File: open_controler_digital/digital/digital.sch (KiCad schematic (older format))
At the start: 20 parts, among them J1 Conn_02x20_Odd_Even

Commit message: avances en la pcb
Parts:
- removed R? (x2): R, symbol Device:R
- removed U? (x5): PC817, Package_DIP:DIP-4_W7.62mm, symbol Isolator:PC817
- added C?: C, symbol Device:C
- added J?: Conn_01x02, symbol Connector_Generic:Conn_01x02
- added Q?: SSM3J338, symbol mosfet:SSM3J338
- added Q?: BC556, Package_TO_SOT_THT:TO-92_Inline, symbol Transistor_BJT:BC556
- added R? (x3): 2K2, symbol Device:R
- added R?: 7R, symbol Device:R
- added R?: 10K, symbol Device:R
- added U?: PC817, Package_DIP:DIP-4_W7.62mm, symbol Isolator:PC817
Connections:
- net labels added: Vcc_1
- net labels removed: GND_B, OD_00
- wire segments 103 -> 95
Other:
- note removed: "temperature buses"
- moved on the sheet: J?, R?

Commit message: avances en la pcb
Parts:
- added Q?: BC556, Package_TO_SOT_THT:TO-92_Inline, symbol Transistor_BJT:BC556
- added R?: 9R, symbol Device:R
- added R?: xxK, symbol Device:R
- added R?: 120R, symbol Device:R
- R?: value 7R -> 4R
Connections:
- wire segments 95 -> 102
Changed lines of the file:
@@
 P 6700 1050
 F 0 "R?" H 6770 1096 50  0000 L CNN
-F 1 "7R" H 6770 1005 50  0000 L CNN
+F 1 "4R" H 6770 1005 50  0000 L CNN
 F 2 "" V 6630 1050 50  0001 C CNN
 F 3 "~" H 6700 1050 50  0001 C CNN
@@
 	6940 1600 7300 1600
 Connection ~ 6940 1600
+$Comp
+L Transistor_BJT:BC556 Q?
+U 1 1 62AE7003
+P 12590 1090
+F 0 "Q?" H 12500 960 50  0000 L CNN
+F 1 "BC556" H 12700 900 50  0000 L CNN
+F 2 "Package_TO_SOT_THT:TO-92_Inline" H 12790 1015 50  0001 L CIN
+F 3 "http://www.fairchildsemi.com/ds/BC/BC557.pdf" H 12590 1090 50  0001 L CNN
+	1    12590 1090
+	-1   0    0    1
+$EndComp
+$Comp
+L Device:R R?
+U 1 1 62AE7009
+P 12790 940
+F 0 "R?" H 12890 990 50  0000 L CNN
+F 1 "9R" H 12890 890 50  0000 L CNN
+F 2 "" V 12720 940 50  0001 C CNN
+F 3 "~" H 12790 940 50  0001 C CNN
+	1    12790 940
+	1    0    0    -1
+$EndComp
+Wire Wire Line
+	12490 890  12490 790
+Wire Wire Line
+	12490 790  12790 790
+Connection ~ 12490 790
+$Comp
+L Device:R R?
+U 1 1 62AE7021
+P 12790 1240
+F 0 "R?" H 12890 1260 50  0000 L CNN
+F 1 "xxK" H 12900 1170 50  0000 L CNN
+F 2 "" V 12720 1240 50  0001 C CNN
+F 3 "~" H 12790 1240 50  0001 C CNN
+	1    12790 1240
+	1    0    0    -1
+$EndComp
+Text GLabel 12490 1790 0    50   Input ~ 0
+GND_1
+Wire Wire Line
+	12490 790  12490 600
+Text GLabel 12490 600  0    50   Input ~ 0
+Vcc_1
+$Comp
+L Device:R R?
+U 1 1 62AE7034
+P 12490 1440
+F 0 "R?" H 12240 1510 50  0000 L CNN
+F 1 "120R" H 12220 1410 50  0000 L CNN
+F 2 "" V 12420 1440 50  0001 C CNN
+F 3 "~" H 12490 1440 50  0001 C CNN
+	1    12490 1440
+	1    0    0    -1
+$EndComp
+Connection ~ 12790 1090
+Wire Wire Line
+	12490 1590 12490 1640
+Wire Wire Line
+	12790 1390 12790 1640
+Wire Wire Line
+	12490 1640 12790 1640
+Wire Wire Line
+	12490 1640 12490 1790
+Connection ~ 12490 1640
 $EndSCHEMATC

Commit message: desarrollando hw, limitador de intensidad
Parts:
- removed Q?: SSM3J338, symbol mosfet:SSM3J338
- removed Q?: BC556, Package_TO_SOT_THT:TO-92_Inline, symbol Transistor_BJT:BC556
- removed R? (x4): R, symbol Device:R
- removed R? (x2): 2K2, symbol Device:R
- added C? (x7): C, symbol Device:C
- added D? (x9): BZT52Bxx, Diode_SMD:D_SOD-123, symbol Diode:BZT52Bxx
- added Q? (x8): BC856, Package_TO_SOT_SMD:SOT-23, symbol Transistor_BJT:BC856
- added Q? (x8): VP0610T, Package_TO_SOT_SMD:SOT-23, symbol Transistor_FET:VP0610T
- added R? (x17): 2K2, symbol Device:R
- added R? (x7): 4R, symbol Device:R
- added R? (x7): 10K, symbol Device:R
- added U? (x8): PC817, Package_DIP:DIP-4_W7.62mm, symbol Isolator:PC817
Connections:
- wire segments 102 -> 243
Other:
- note added: "La resistencia elevada para que el consumo , en condiciones normales de trabajo, sea bajo\nResistencia baja para asegurar la estabilidad del circuito y eliminar efectos de ruido\nEl Zener puede ir desde 3,5V a 20V que es el maximo de sopore de jmosfet"
- moved on the sheet: C?, J1, J?, R?, U?

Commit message: avanzando con el limitador de intensidad
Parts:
- removed C? (x5): C, symbol Device:C
- removed D? (x9): BZT52Bxx, Diode_SMD:D_SOD-123, symbol Diode:BZT52Bxx
- removed Q?: BC556, Package_TO_SOT_THT:TO-92_Inline, symbol Transistor_BJT:BC556
- removed Q? (x5): BC856, Package_TO_SOT_SMD:SOT-23, symbol Transistor_BJT:BC856
- removed Q? (x5): VP0610T, Package_TO_SOT_SMD:SOT-23, symbol Transistor_FET:VP0610T
- removed R? (x6): R, symbol Device:R
- removed R?: 9R, symbol Device:R
- removed R?: xxK, symbol Device:R
- removed R?: 120R, symbol Device:R
- removed R? (x12): 2K2, symbol Device:R
- removed R? (x5): 4R, symbol Device:R
- removed R? (x5): 10K, symbol Device:R
- removed U? (x6): PC817, Package_DIP:DIP-4_W7.62mm, symbol Isolator:PC817
- added C? (x3): C, symbol Device:C
- added Q? (x3): BC856, Package_TO_SOT_SMD:SOT-23, symbol Transistor_BJT:BC856
- added Q? (x3): VP0610T, Package_TO_SOT_SMD:SOT-23, symbol Transistor_FET:VP0610T
- added R? (x9): 10K, symbol Device:R
- added R? (x16): 4K7, symbol Device:R
- added R? (x6): 2K2, symbol Device:R
- added R? (x3): 7R, symbol Device:R
- added U? (x11): PC817, Package_DIP:DIP-4_W7.62mm, symbol Isolator:PC817
- J?: value Conn_01x10 -> d_o_01x10
- J?: value Conn_01x10 -> d_i_01x10
- R? (x3): value 4R -> 7R
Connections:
- net labels added: GND_xx, GPIO_xx, d_i_0, d_i_1, d_i_2, d_i_3, d_i_4, d_i_5, d_o_0, d_o_1, d_o_2, d_o_3, d_o_4, d_o_5, id_xx
- wire segments 243 -> 168
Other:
- note removed: "La resistencia elevada para que el consumo , en condiciones normales de trabajo, sea bajo\nResistencia baja para asegurar la estabilidad del circuito y eliminar efectos de ruido\nEl Zener puede ir desde 3,5V a 20V que es el maximo de sopore de jmosfet"
- moved on the sheet: C?, J?, Q?, R?, U?

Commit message: avances pcb digital
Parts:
- removed C?: C, symbol Device:C
- removed Q?: BC856, Package_TO_SOT_SMD:SOT-23, symbol Transistor_BJT:BC856
- removed Q?: VP0610T, Package_TO_SOT_SMD:SOT-23, symbol Transistor_FET:VP0610T
- removed R? (x2): 10K, symbol Device:R
- removed R? (x2): 2K2, symbol Device:R
- removed R?: 7R, symbol Device:R
- removed R? (x6): 4K7, symbol Device:R
- removed U? (x4): PC817, Package_DIP:DIP-4_W7.62mm, symbol Isolator:PC817
- added C2, C7: C, Capacitor_SMD:C_1206_3216Metric_Pad1.42x1.75mm_HandSolder, symbol Device:C
- added D1: D_Schottky, Diode_SMD:D_2114_3652Metric, symbol Device:D_Schottky
- added Q2: BC856, Package_TO_SOT_SMD:SOT-23, symbol Transistor_BJT:BC856
- added Q4: VP0610T, Package_TO_SOT_SMD:SOT-23, symbol Transistor_FET:VP0610T
- added R10: 1K5, Resistor_SMD:R_1206_3216Metric_Pad1.42x1.75mm_HandSolder, symbol Device:R
- added R2: 7R, Resistor_SMD:R_1206_3216Metric_Pad1.42x1.75mm_HandSolder, symbol Device:R
- added R36, R42: 4K7, Resistor_SMD:R_1206_3216Metric_Pad1.42x1.75mm_HandSolder, symbol Device:R
- added R4, R8: 10K, Resistor_SMD:R_1206_3216Metric_Pad1.42x1.75mm_HandSolder, symbol Device:R
- added R6: 1K2, Resistor_SMD:R_1206_3216Metric_Pad1.42x1.75mm_HandSolder, symbol Device:R
- added U12, U2: PC817, Package_DIP:DIP-4_W8.89mm_SMDSocket_LongPads, symbol Isolator:PC817
- C1, C3, C4, C5, C6: renamed from C?; footprint (none) -> Capacitor_SMD:C_1206_3216Metric_Pad1.42x1.75mm_HandSolder
- J1, J2: renamed from J?; footprint (none) -> Connector_Phoenix_MC:PhoenixContact_MCV_1,5_10-G-3.5_1x10_P3.50mm_Vertical
- J4: renamed from J?; footprint (none) -> Connector_Phoenix_MC:PhoenixContact_MCV_1,5_2-G-3.5_1x02_P3.50mm_Vertical
- R1, R11, R12, R13, R14, R15, R16, R17, R18, R23, R24, R25, R26, R27, R28, R29, R3, R30, R31, R32, R33, R34, R35, R37, R38, R39, R40, R41, R7: renamed from R?; footprint (none) -> Resistor_SMD:R_1206_3216Metric_Pad1.42x1.75mm_HandSolder
- R19, R20, R21, R22, R5: renamed from R?; value 2K2 -> 1K2; footprint (none) -> Resistor_SMD:R_1206_3216Metric_Pad1.42x1.75mm_HandSolder
- R9: renamed from R?; value 2K2 -> 1K5; footprint (none) -> Resistor_SMD:R_1206_3216Metric_Pad1.42x1.75mm_HandSolder
- U1, U10, U11, U3, U4, U5, U6, U7, U8, U9: renamed from U?; footprint Package_DIP:DIP-4_W7.62mm -> Package_DIP:DIP-4_W8.89mm_SMDSocket_LongPads
- gave numbers to parts that had none: 10
- renumbered J1 to J3
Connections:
- net labels added: di20, di21, di22, di30, di31, di32, do00, do01, do02, do10, do11, do12, gi2, gi3, go0, go1, vo0, vo1
- net labels removed: 3v3_1, 3v3_2, GND_xx, GPIO_0, GPIO_1, GPIO_10, GPIO_11, GPIO_14, GPIO_15, GPIO_17, GPIO_2, GPIO_21, GPIO_3, GPIO_4, GPIO_7, GPIO_8, GPIO_9, GPIO_xx, Vcc_1, d_i_0, d_i_1, d_i_2, d_i_3, d_i_4, d_i_5, d_o_0, d_o_1, d_o_2, d_o_3, d_o_4, d_o_5, id_xx
- wire segments 168 -> 169
- no-connect marks 2 -> 18
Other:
- note added: "3v3"
- note added: "3v3_1"
- note added: "5V"
- note added: "GND"
- note added: "GPIO0"
- note added: "GPIO_1"
- note added: "GPIO_10"
- note added: "GPIO_11"
- note added: "GPIO_12"
- note added: "GPIO_13"
- note added: "GPIO_14"
- note added: "GPIO_15"
- note added: "GPIO_16"
- note added: "GPIO_17"
- note added: "GPIO_18"
- note added: "GPIO_19"
- note added: "GPIO_2"
- note added: "GPIO_20"
- note added: "GPIO_21"
- note added: "GPIO_22"
- note added: "GPIO_23"
- note added: "GPIO_24"
- note added: "GPIO_25"
- note added: "GPIO_3"
- note added: "GPIO_4"
- note added: "GPIO_5"
- note added: "GPIO_6"
- note added: "GPIO_7"
- note added: "GPIO_8"
- note added: "GPIO_9"
- note added: "IOT_0"
- note added: "IOT_1"
- moved on the sheet: C6, J1, J2, J4, Q12, Q8, R14, R18, R22, R26, R30, R35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

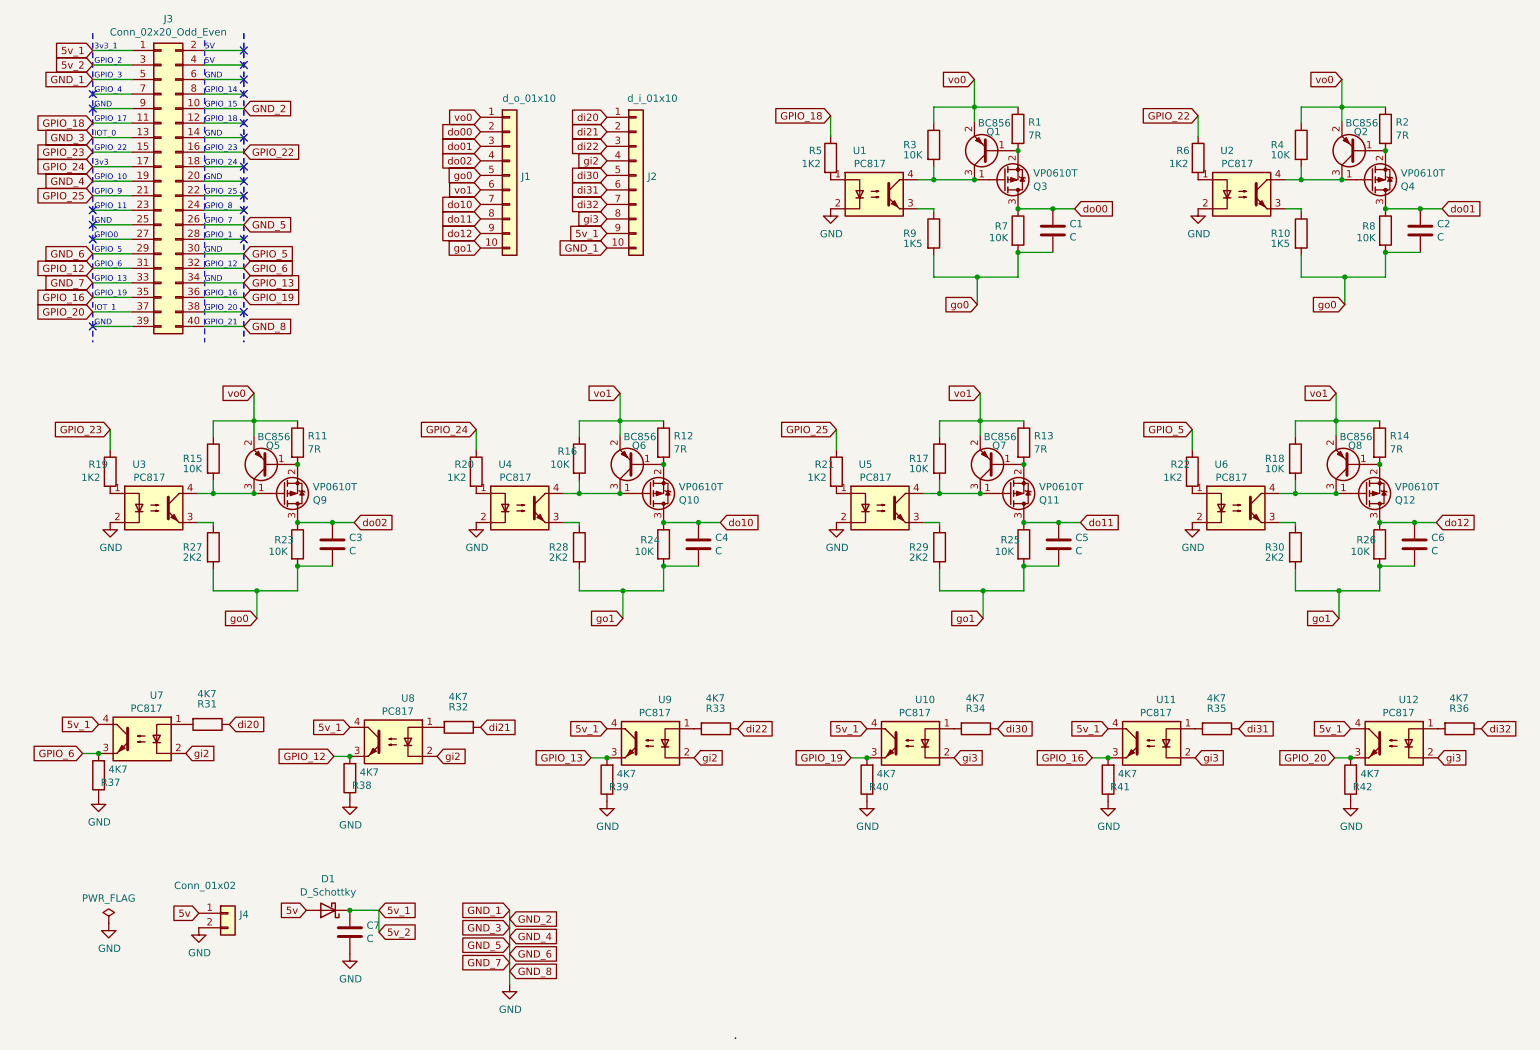
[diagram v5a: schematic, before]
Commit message: desarrollo de la PCB con la huella de la Raspberry
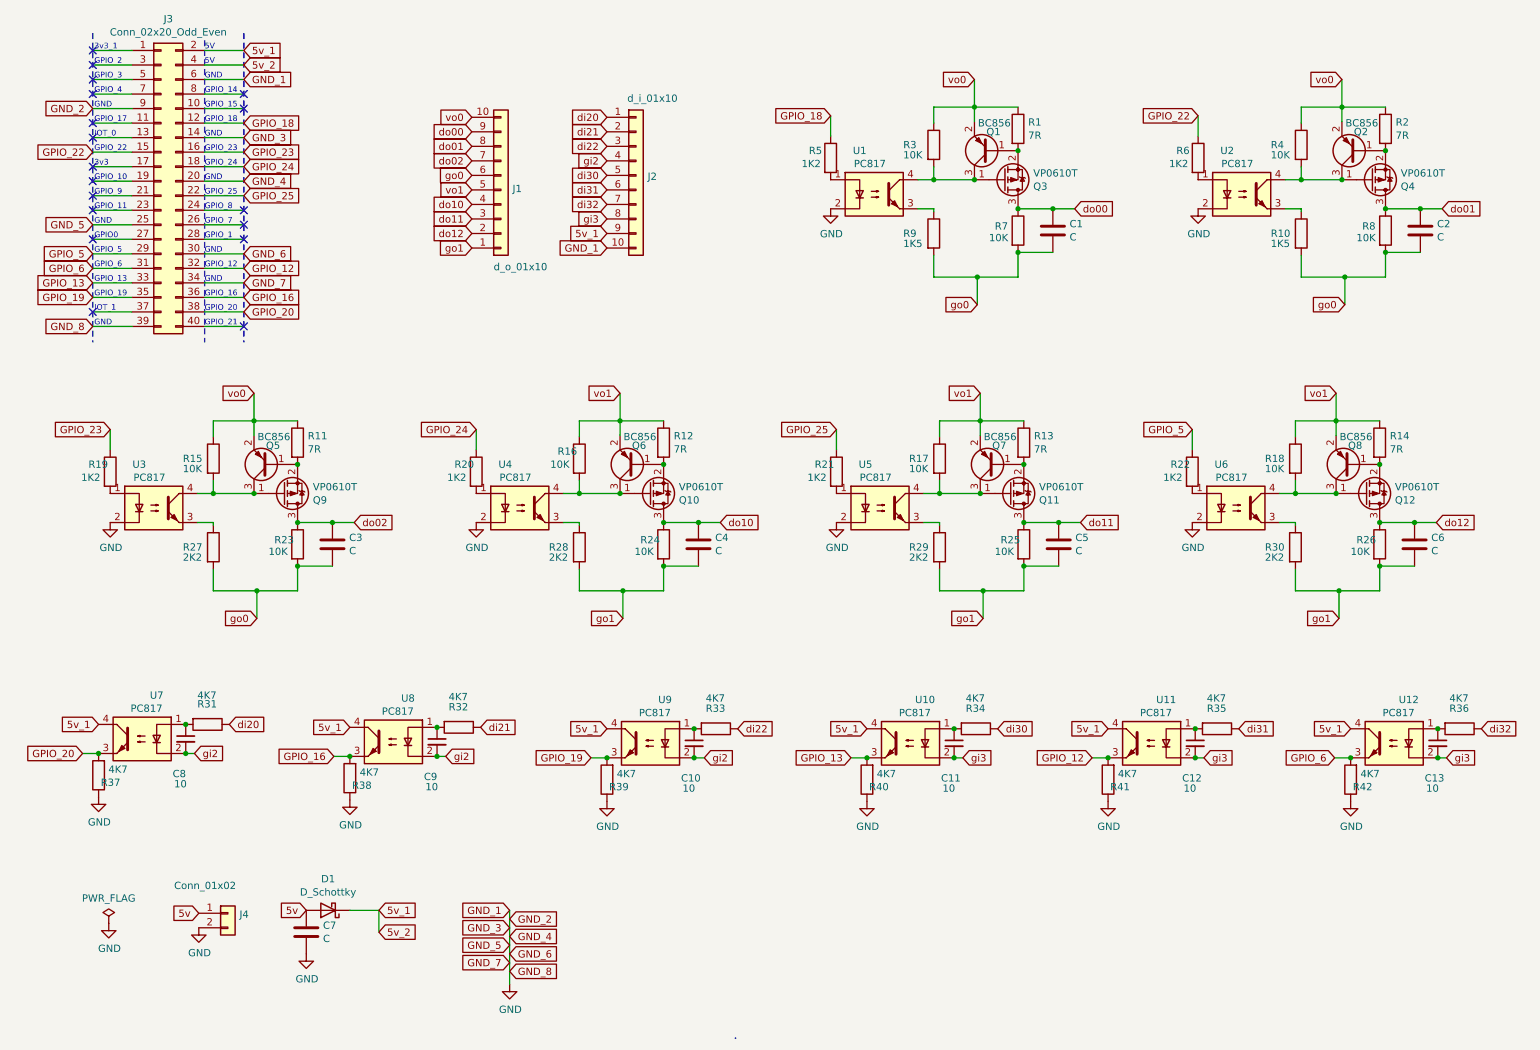
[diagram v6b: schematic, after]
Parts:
- added C10, C11, C12, C13, C8, C9: 10, Capacitor_SMD:C_1206_3216Metric_Pad1.42x1.75mm_HandSolder, symbol Device:C_Small
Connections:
- wire segments 169 -> 175
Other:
- moved on the sheet: C7, J1

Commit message: version para fabricacion
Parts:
- C1, C2, C3, C4, C5, C6, C7: value C -> 10
- Q10, Q11, Q12, Q3, Q4, Q9: value VP0610T -> JM
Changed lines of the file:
@@
 P 7700 2050
 F 0 "C1" H 7815 2096 50  0000 L CNN
-F 1 "C" H 7815 2005 50  0000 L CNN
+F 1 "10" H 7815 2005 50  0000 L CNN
 F 2 "Capacitor_SMD:C_1206_3216Metric_Pad1.42x1.75mm_HandSolder" H 7738 1900 50  0001 C CNN
 F 3 "~" H 7700 2050 50  0001 C CNN
@@
 P 7360 1700
 F 0 "Q3" H 7565 1746 50  0000 L CNN
-F 1 "VP0610T" H 7565 1655 50  0000 L CNN
+F 1 "JM" H 7565 1655 50  0000 L CNN
 F 2 "Package_TO_SOT_SMD:SOT-23" H 7560 1625 50  0001 L CIN
 F 3 "http://www.vishay.com/docs/70209/70209.pdf" H 7360 1700 50  0001 L CNN
@@
 P 2740 4210
 F 0 "C3" H 2855 4256 50  0000 L CNN
-F 1 "C" H 2855 4165 50  0000 L CNN
+F 1 "10" H 2855 4165 50  0000 L CNN
 F 2 "Capacitor_SMD:C_1206_3216Metric_Pad1.42x1.75mm_HandSolder" H 2778 4060 50  0001 C CNN
 F 3 "~" H 2740 4210 50  0001 C CNN
@@
 P 2400 3860
 F 0 "Q9" H 2605 3906 50  0000 L CNN
-F 1 "VP0610T" H 2605 3815 50  0000 L CNN
+F 1 "JM" H 2605 3815 50  0000 L CNN
 F 2 "Package_TO_SOT_SMD:SOT-23" H 2600 3785 50  0001 L CIN
 F 3 "http://www.vishay.com/docs/70209/70209.pdf" H 2400 3860 50  0001 L CNN
@@
 P 4920 3860
 F 0 "Q10" H 5125 3906 50  0000 L CNN
-F 1 "VP0610T" H 5125 3815 50  0000 L CNN
+F 1 "JM" H 5125 3815 50  0000 L CNN
 F 2 "Package_TO_SOT_SMD:SOT-23" H 5120 3785 50  0001 L CIN
 F 3 "http://www.vishay.com/docs/70209/70209.pdf" H 4920 3860 50  0001 L CNN
@@
 P 5260 4210
 F 0 "C4" H 5375 4256 50  0000 L CNN
-F 1 "C" H 5375 4165 50  0000 L CNN
+F 1 "10" H 5375 4165 50  0000 L CNN
 F 2 "Capacitor_SMD:C_1206_3216Metric_Pad1.42x1.75mm_HandSolder" H 5298 4060 50  0001 C CNN
 F 3 "~" H 5260 4210 50  0001 C CNN
@@
 P 7400 3860
 F 0 "Q11" H 7605 3906 50  0000 L CNN
-F 1 "VP0610T" H 7605 3815 50  0000 L CNN
+F 1 "JM" H 7605 3815 50  0000 L CNN
 F 2 "Package_TO_SOT_SMD:SOT-23" H 7600 3785 50  0001 L CIN
 F 3 "http://www.vishay.com/docs/70209/70209.pdf" H 7400 3860 50  0001 L CNN
@@
 P 7740 4210
 F 0 "C5" H 7855 4256 50  0000 L CNN
-F 1 "C" H 7855 4165 50  0000 L CNN
+F 1 "10" H 7855 4165 50  0000 L CNN
 F 2 "Capacitor_SMD:C_1206_3216Metric_Pad1.42x1.75mm_HandSolder" H 7778 4060 50  0001 C CNN
 F 3 "~" H 7740 4210 50  0001 C CNN
@@
 P 9850 3860
 F 0 "Q12" H 10055 3906 50  0000 L CNN
-F 1 "VP0610T" H 10055 3815 50  0000 L CNN
+F 1 "JM" H 10055 3815 50  0000 L CNN
 F 2 "Package_TO_SOT_SMD:SOT-23" H 10050 3785 50  0001 L CIN
 F 3 "http://www.vishay.com/docs/70209/70209.pdf" H 9850 3860 50  0001 L CNN
@@
 P 10190 4210
 F 0 "C6" H 10305 4256 50  0000 L CNN
-F 1 "C" H 10305 4165 50  0000 L CNN
+F 1 "10" H 10305 4165 50  0000 L CNN
 F 2 "Capacitor_SMD:C_1206_3216Metric_Pad1.42x1.75mm_HandSolder" H 10228 4060 50  0001 C CNN
 F 3 "~" H 10190 4210 50  0001 C CNN
@@
 P 10230 2050
 F 0 "C2" H 10345 2096 50  0000 L CNN
-F 1 "C" H 10345 2005 50  0000 L CNN
+F 1 "10" H 10345 2005 50  0000 L CNN
 F 2 "Capacitor_SMD:C_1206_3216Metric_Pad1.42x1.75mm_HandSolder" H 10268 1900 50  0001 C CNN
 F 3 "~" H 10230 2050 50  0001 C CNN
@@
 P 9890 1700
 F 0 "Q4" H 10095 1746 50  0000 L CNN
-F 1 "VP0610T" H 10095 1655 50  0000 L CNN
+F 1 "JM" H 10095 1655 50  0000 L CNN
 F 2 "Package_TO_SOT_SMD:SOT-23" H 10090 1625 50  0001 L CIN
 F 3 "http://www.vishay.com/docs/70209/70209.pdf" H 9890 1700 50  0001 L CNN
@@
 P 2560 6880
 F 0 "C7" H 2675 6926 50  0000 L CNN
-F 1 "C" H 2675 6835 50  0000 L CNN
+F 1 "10" H 2675 6835 50  0000 L CNN
 F 2 "Capacitor_SMD:C_1206_3216Metric_Pad1.42x1.75mm_HandSolder" H 2598 6730 50  0001 C CNN
 F 3 "~" H 2560 6880 50  0001 C CNN
